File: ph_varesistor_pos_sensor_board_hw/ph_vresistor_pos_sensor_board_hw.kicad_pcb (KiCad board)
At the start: 2 copper layers, 46.4 x 22.2 mm, 16 parts, among them J1 Conn_01x02, J2 Varesistor, U1 LM317_TO3

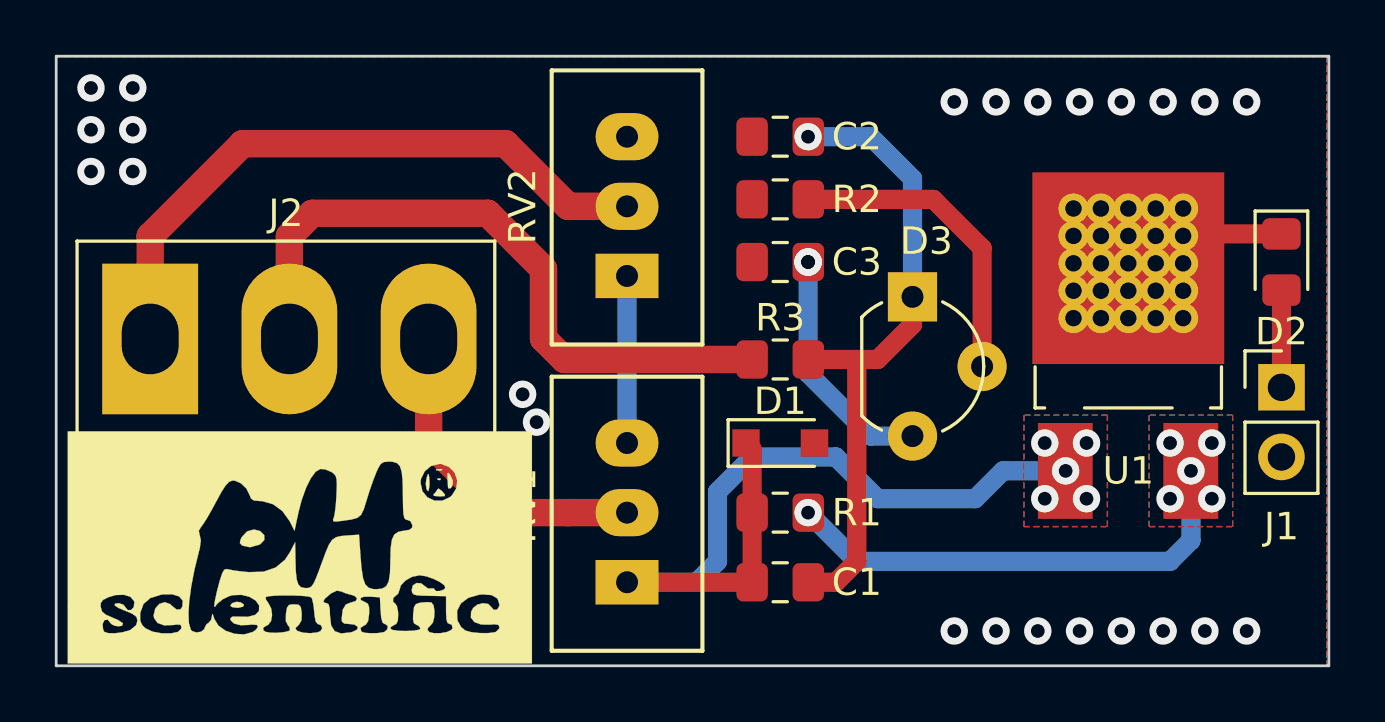
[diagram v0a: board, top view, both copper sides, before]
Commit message: Layout board varesistor is finished
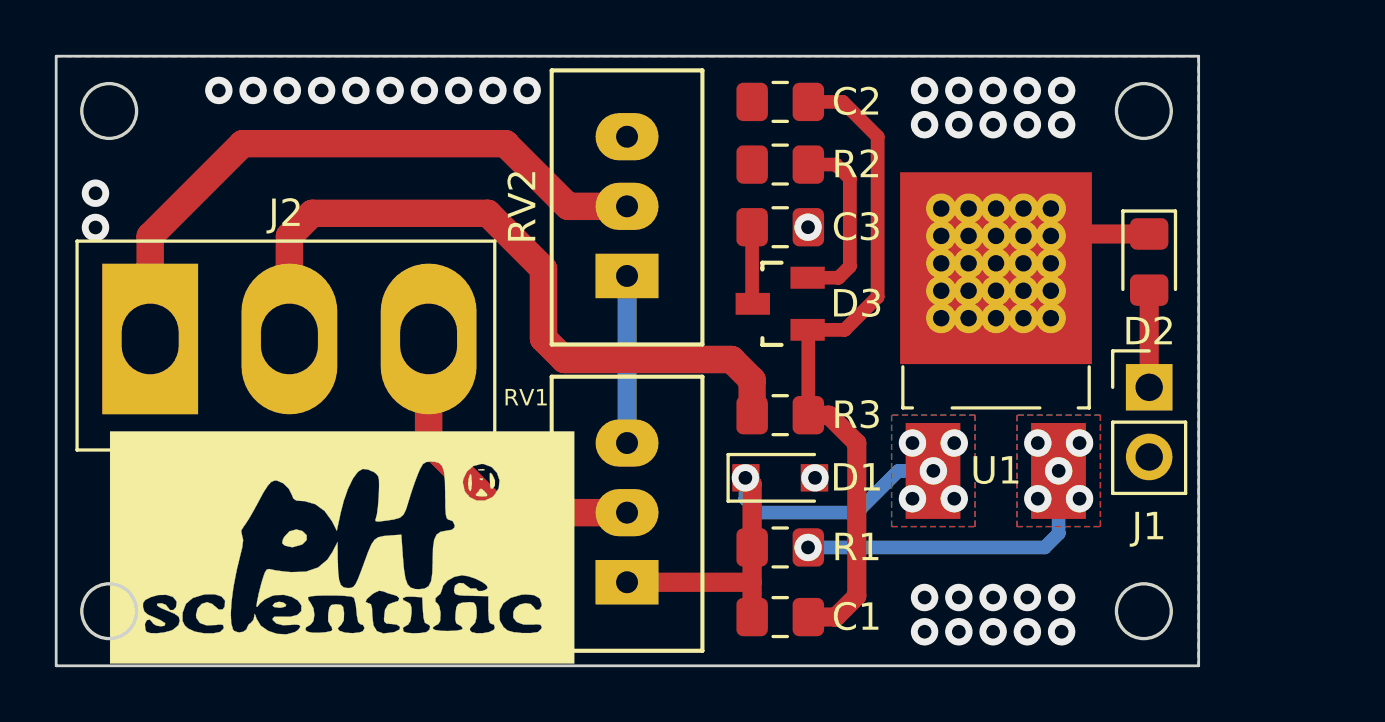
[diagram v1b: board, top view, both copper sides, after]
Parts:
- D3: footprint VinhTho_Lib:TO-92_Molded_Wide -> VinhTho_Lib:SOT-23
- moved D3 4.83 mm to (110.0, 81.5), turned to 90 degrees
- moved D2 4.83 mm to (123.4, 80.0)
- moved J1 4.83 mm to (123.4, 84.6)
- moved U1 4.83 mm to (117.9, 83.1)
- moved R3 2.03 mm to (110.0, 85.6)
- moved G*** 1.54 mm to (94.0, 90.4) (x2)
- moved C3 1.27 mm to (110.0, 78.7), turned to 0 degrees
- moved R1 1.27 mm to (110.0, 90.4)
- moved R2 1.27 mm to (110.0, 76.5)
- moved C1 1.27 mm to (110.0, 93.0)
- moved C2 1.27 mm to (110.0, 74.2)
- moved D1 1.27 mm to (110.0, 87.9)
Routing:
- net Net-(C1-Pad1): track 30.2 -> 18.2 mm, vias 5 -> 6
- net Net-(C3-Pad1): track 8.82 -> 2.81 mm, vias 2 -> 0
- net Net-(R1-Pad1): track 17.6 -> 11.6 mm
- net Net-(D3-Pad2): track 11.4 -> 6.65 mm
- net Net-(J2-Pad2): track 24.7 -> 26.3 mm
- net Net-(C1-Pad2): track 23.6 -> 24.9 mm, vias 1 -> 0
- net GND: track 0.01 -> 0.00 mm, vias 24 -> 34
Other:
- board size 46.4 x 22.2 mm -> 41.7 x 22.2 mm
- board text added: "+24V"
- board text added: "GND"
